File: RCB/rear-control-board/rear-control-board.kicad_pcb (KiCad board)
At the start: 2 copper layers, 99.1 x 99.1 mm, 55 parts, among them J1 Conn_01x23, J2 Conn_01x14, J3 Conn_01x08, J4 Conn_01x02, J5 Conn_01x02, J6 Conn_01x05, K1 T9VV1K15-12S, K2 G5V-2, K3 G5V-2, Q1 BSS84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

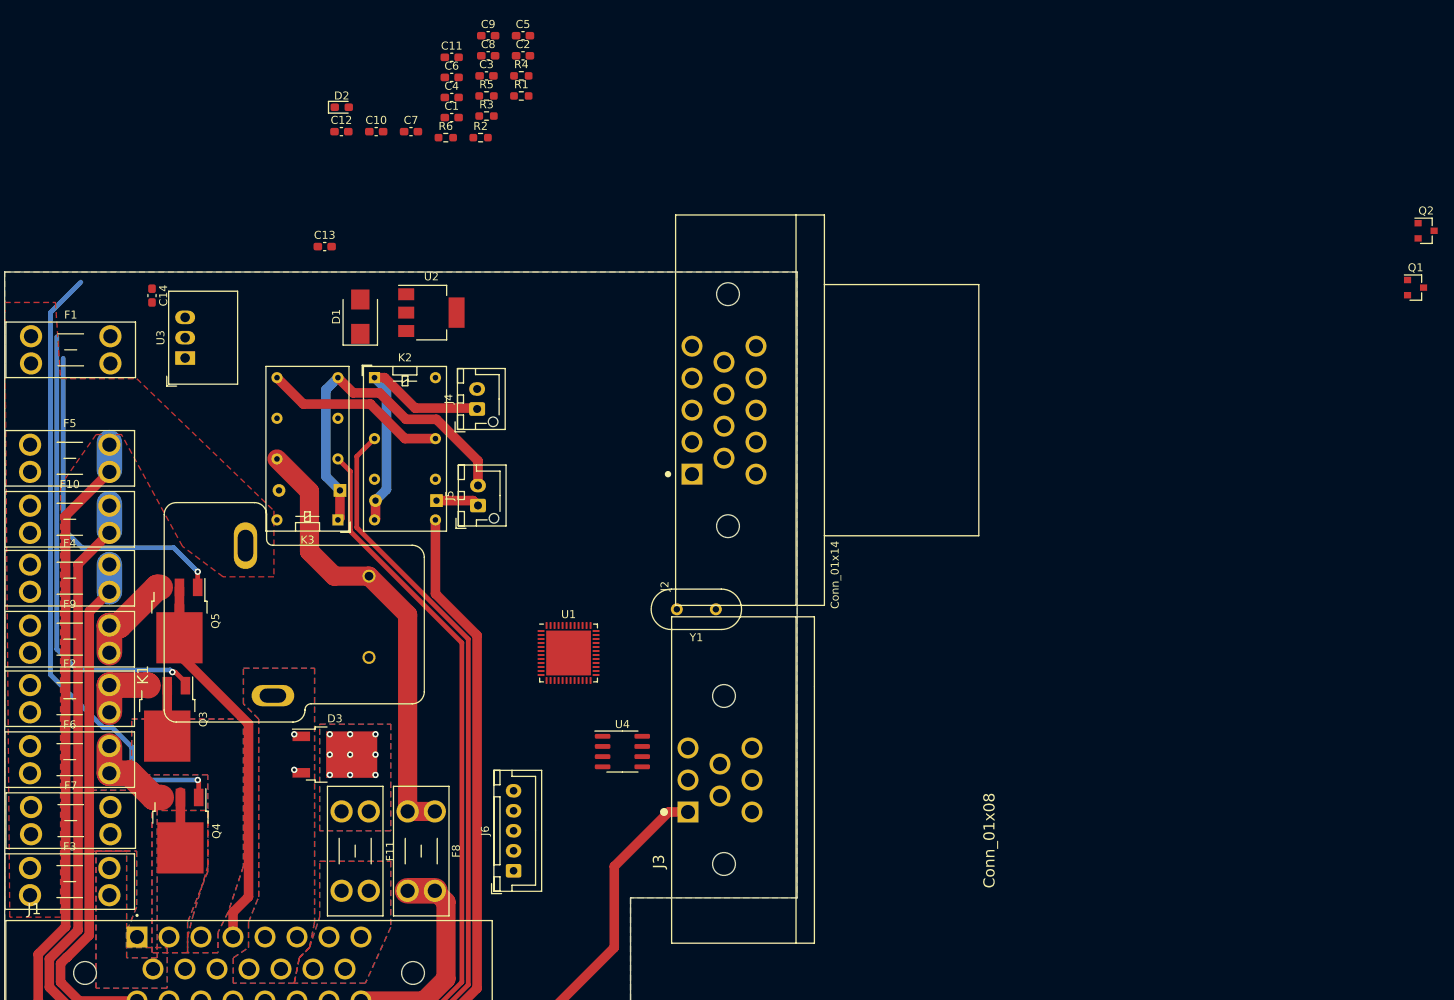
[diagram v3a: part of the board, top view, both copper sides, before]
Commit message: finishing layout placement
Still need to route wires
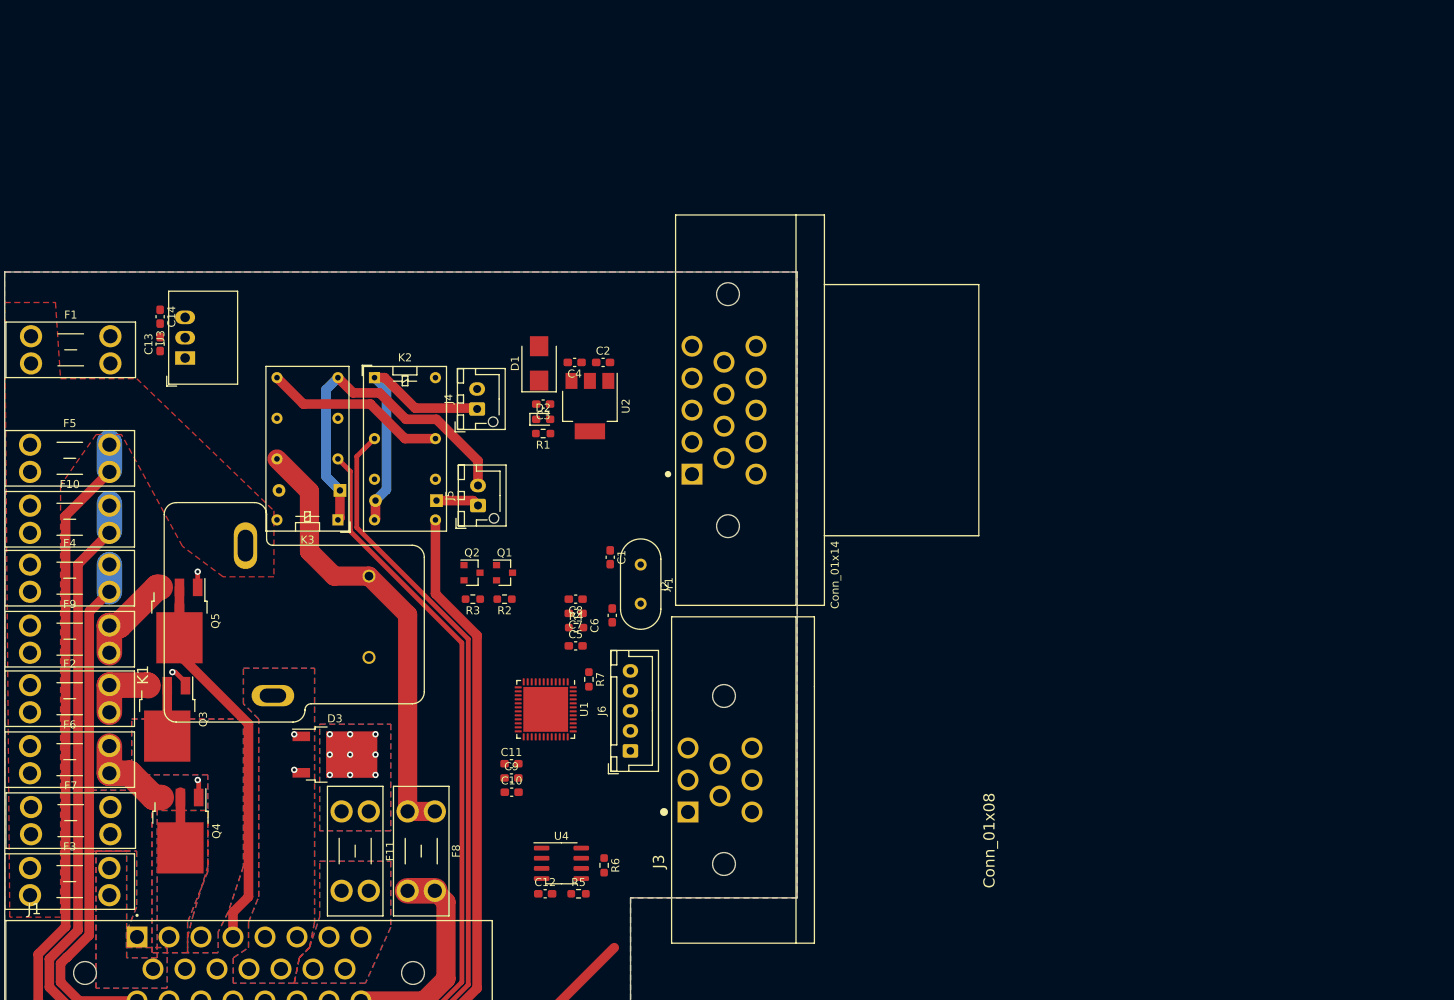
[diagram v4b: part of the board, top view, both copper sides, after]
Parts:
- added R7: 10k, Resistor_SMD:R_0603_1608Metric_Pad0.98x0.95mm_HandSolder, F.Cu at (134.0, 91.6)
- moved Q2 126.7 mm to (119.4, 78.2)
- moved Q1 119.3 mm to (123.4, 78.2)
- moved R5 100.4 mm to (132.7, 118.4)
- moved C12 98.6 mm to (128.5, 118.4)
- moved R6 93.1 mm to (135.9, 114.8), turned to -90 degrees
- moved C9 92.8 mm to (124.3, 103.9)
- moved C11 88.6 mm to (124.3, 102.1)
- moved C10 84.3 mm to (124.3, 105.7)
- moved C5 76.6 mm to (132.3, 87.4)
- moved C6 70.2 mm to (136.9, 83.6), turned to 90 degrees
- moved R4 69.3 mm to (132.4, 85.1)
- moved C8 68.8 mm to (132.3, 81.5), turned to 180 degrees
- moved C7 63.6 mm to (132.3, 83.3), turned to 180 degrees
- moved R3 60.4 mm to (119.5, 81.5), turned to 180 degrees
- moved C1 58.4 mm to (136.7, 76.3), turned to -90 degrees
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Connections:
- J2 pad 1: GND -> /WHEEL_L
- J2 pad 10: /WHEEL_L -> GND
- J2 pad 11: VDD -> GND
- J2 pad 12: VDD -> GND
- J2 pad 13: VDD -> GND
- J2 pad 2: GND -> /WHEEL_R
- J2 pad 3: GND -> +3V3
- J2 pad 4: GND -> VDD
- J2 pad 5: unconnected-(J2-Pad5) -> VDD
- J2 pad 6: /TEMP_WATER -> /TEMP_WATER-
- J2 pad 7: /SUSPENSION_R -> /SUSPENSION_L
- J2 pad 8: /SUSPENSION_L -> /SUSPENSION_R
- J2 pad 9: /WHEEL_R -> VDD
- R2 pad 2: /Controller/FAULT_IMD -> /Controller/FAULT_BMS
- R3 pad 1: /Controller/FAULT_BMS -> /Controller/FAULT_IMD
- U1 pad 14: /Controller/FAN_CTRL -> /Controller/BRAKE_CTRL
- U1 pad 15: /Controller/PUMP_CTRL -> /Controller/FAN_CTRL
- U1 pad 16: /Controller/BRAKE_CTRL -> /Controller/PUMP_CTRL
- U1 pad 17: /Controller/NTC1 -> unconnected-(U1-Pad17)
- U1 pad 18: unconnected-(U1-Pad18) -> /Controller/FAULT_BMS
- U1 pad 19: unconnected-(U1-Pad19) -> /Controller/FAULT_IMD
- U1 pad 2: unconnected-(U1-Pad2) -> /TEMP_WATER-
- U1 pad 32: unconnected-(U1-Pad32) -> /Controller/CAN_X_P
- U1 pad 33: unconnected-(U1-Pad33) -> /Controller/CAN_X_N
- U1 pad 43: /Controller/FAULT_IMD -> unconnected-(U1-Pad43)
- U1 pad 45: /Controller/FAULT_BMS -> unconnected-(U1-Pad45)
- U4 pad 1: /Controller/CAN_TX_P -> /Controller/CAN_X_P
- U4 pad 4: /Controller/CAN_RX_N -> /Controller/CAN_X_N
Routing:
- net /Controller/PUMP_CTRL: track 78.0 -> 2.23 mm
- net /Controller/FAN_CTRL: track 57.3 -> 2.64 mm
- net /Controller/BRAKE_CTRL: track 42.3 -> 1.96 mm
- net /HVB_12V: track 175.7 -> 153.6 mm

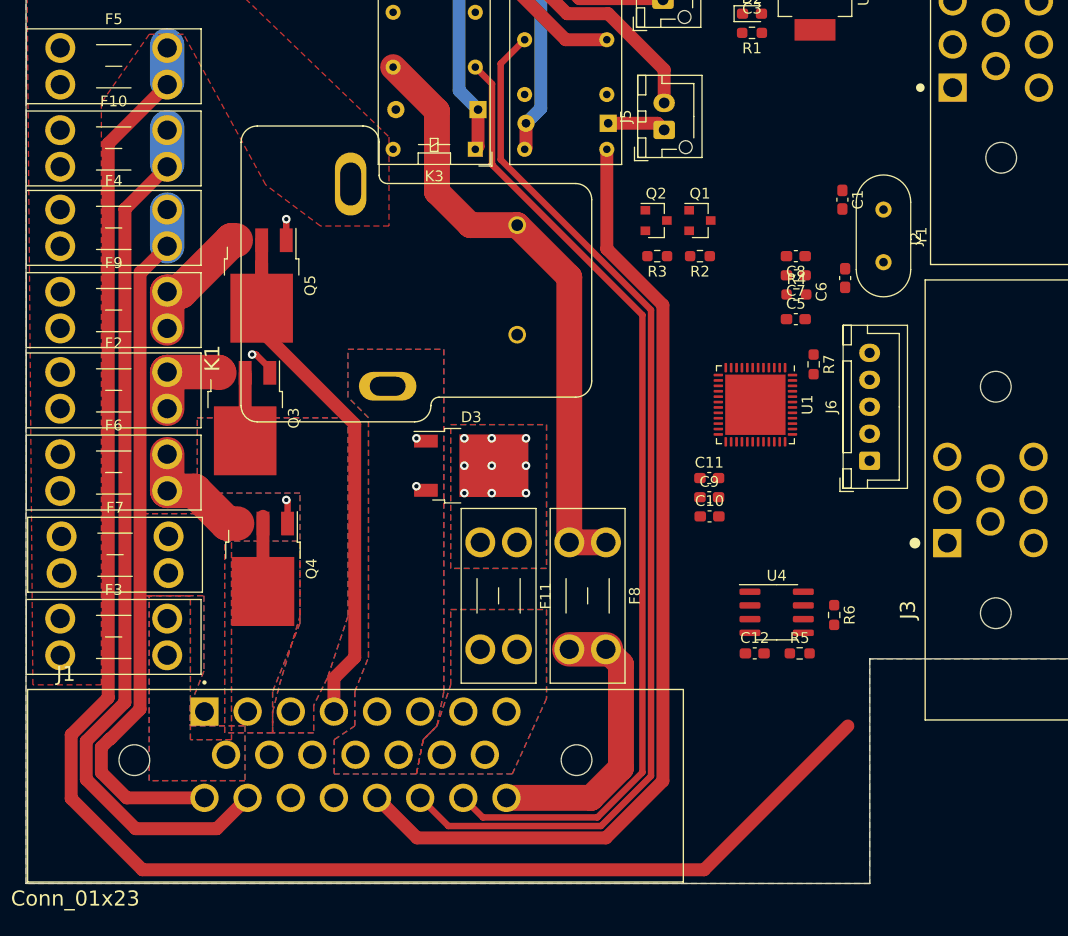
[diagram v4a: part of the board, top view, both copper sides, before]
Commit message: adjusting pinout, updating layout
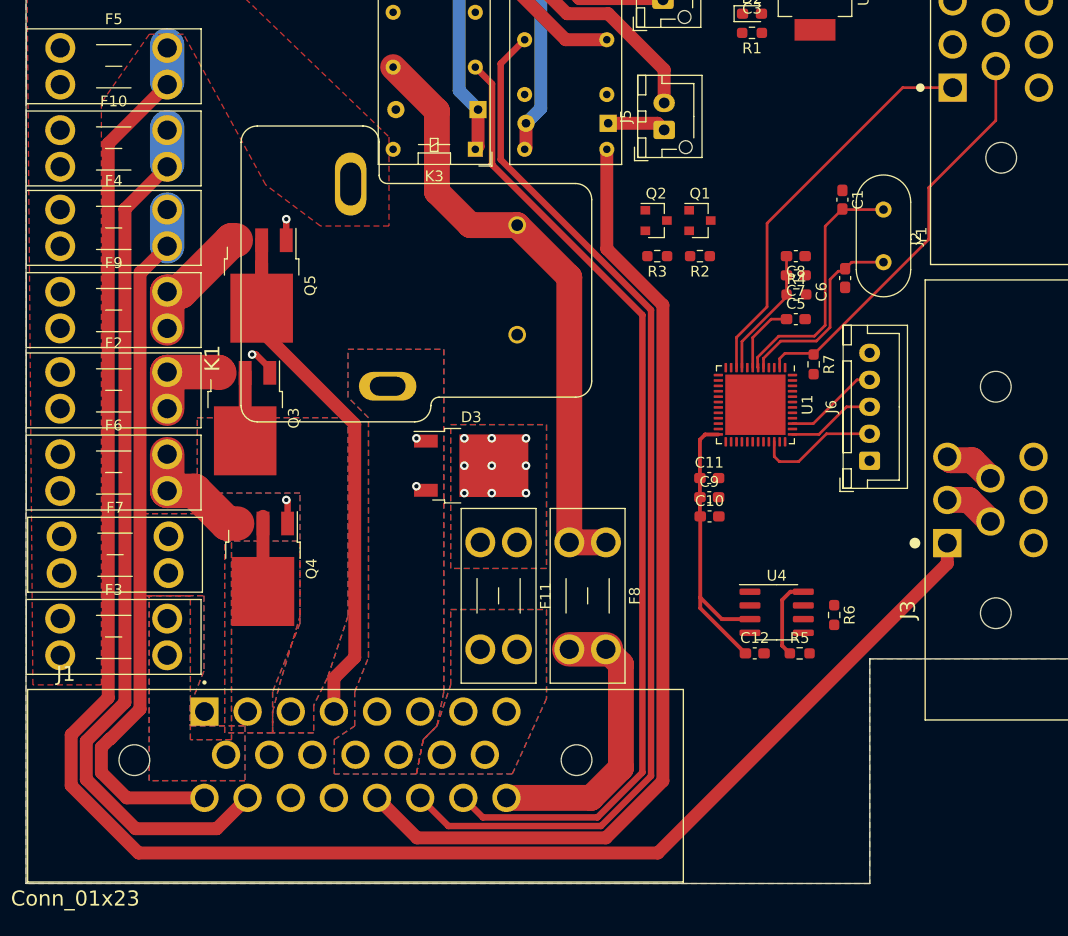
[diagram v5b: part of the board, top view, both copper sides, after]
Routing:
- net /TEMP_WATER-: track 0.00 -> 38.0 mm
- net /WHEEL_L: track 0.00 -> 37.0 mm
- net +3V3: track 0.00 -> 28.9 mm
- net Net-(C1-Pad2): track 0.00 -> 23.8 mm
- net Net-(C6-Pad2): track 0.00 -> 18.3 mm
- net /HVB_12V: track 153.6 -> 168.9 mm
- net Net-(C7-Pad2): track 0.00 -> 12.1 mm
- net A13_SWDIO: track 0.00 -> 11.5 mm
- net B3_TRACESWO: track 0.00 -> 8.83 mm
- net A14_SWCLK: track 0.00 -> 8.21 mm
- net Net-(R5-Pad1): track 0.00 -> 7.53 mm
- net Net-(C5-Pad1): track 0.00 -> 6.63 mm
- net /CAN_P: track 0.00 -> 4.83 mm
- net /CAN_N: track 0.00 -> 4.83 mm

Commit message: trace layout complete (need review)
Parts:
- moved Q1 4.56 mm to (119.0, 77.2), turned to 90 degrees
- moved Q2 4.33 mm to (123.7, 78.5)
- moved Y1 3.21 mm to (140.5, 74.0)
- moved R3 1.24 mm to (119.0, 80.4)
- moved C2 1.12 mm to (135.8, 53.1)
- moved C4 1.12 mm to (132.2, 53.1)
- moved U2 1.12 mm to (134.1, 58.5)
- moved C12 0.76 mm to (129.3, 118.4)
- moved C5 0.72 mm to (131.8, 87.9)
- moved R2 0.62 mm to (123.8, 82.0), turned to 0 degrees
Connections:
- R2 pad 2: /Controller/FAULT_BMS -> /Controller/FAULT_IMD
- R3 pad 1: /Controller/FAULT_IMD -> /Controller/FAULT_BMS
- U1 pad 15: /Controller/FAN_CTRL -> /Controller/PUMP_CTRL
- U1 pad 16: /Controller/PUMP_CTRL -> /Controller/FAN_CTRL
- U1 pad 18: /Controller/FAULT_BMS -> /Controller/FAULT_IMD
- U1 pad 19: /Controller/FAULT_IMD -> /Controller/FAULT_BMS
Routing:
- net +3V3: track 28.9 -> 225.5 mm, vias 0 -> 1
- net VDD: track 5.44 -> 119.5 mm
- net /Controller/PUMP_CTRL: track 2.23 -> 74.2 mm, vias 1 -> 2
- net /SUSPENSION_R: track 0.00 -> 48.7 mm
- net /Controller/FAN_CTRL: track 2.64 -> 47.6 mm, vias 1 -> 2
- net /SUSPENSION_L: track 0.00 -> 44.9 mm
- net /Controller/BRAKE_CTRL: track 1.96 -> 45.4 mm, vias 1 -> 2
- net /WHEEL_R: track 0.00 -> 39.3 mm
- net /Controller/FAULT_BMS: track 0.00 -> 23.6 mm
- net /CAN_N: track 4.83 -> 26.1 mm
- net /Controller/FAULT_IMD: track 0.00 -> 21.2 mm
- net /CAN_P: track 4.83 -> 25.8 mm
- net /Controller/CAN_X_N: track 0.00 -> 19.3 mm
- net /Controller/CAN_X_P: track 0.00 -> 19.1 mm
- net /FAULT_LATCHER/bms_switch: track 33.5 -> 50.9 mm
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- added copper zone on B.Cu, net +12V

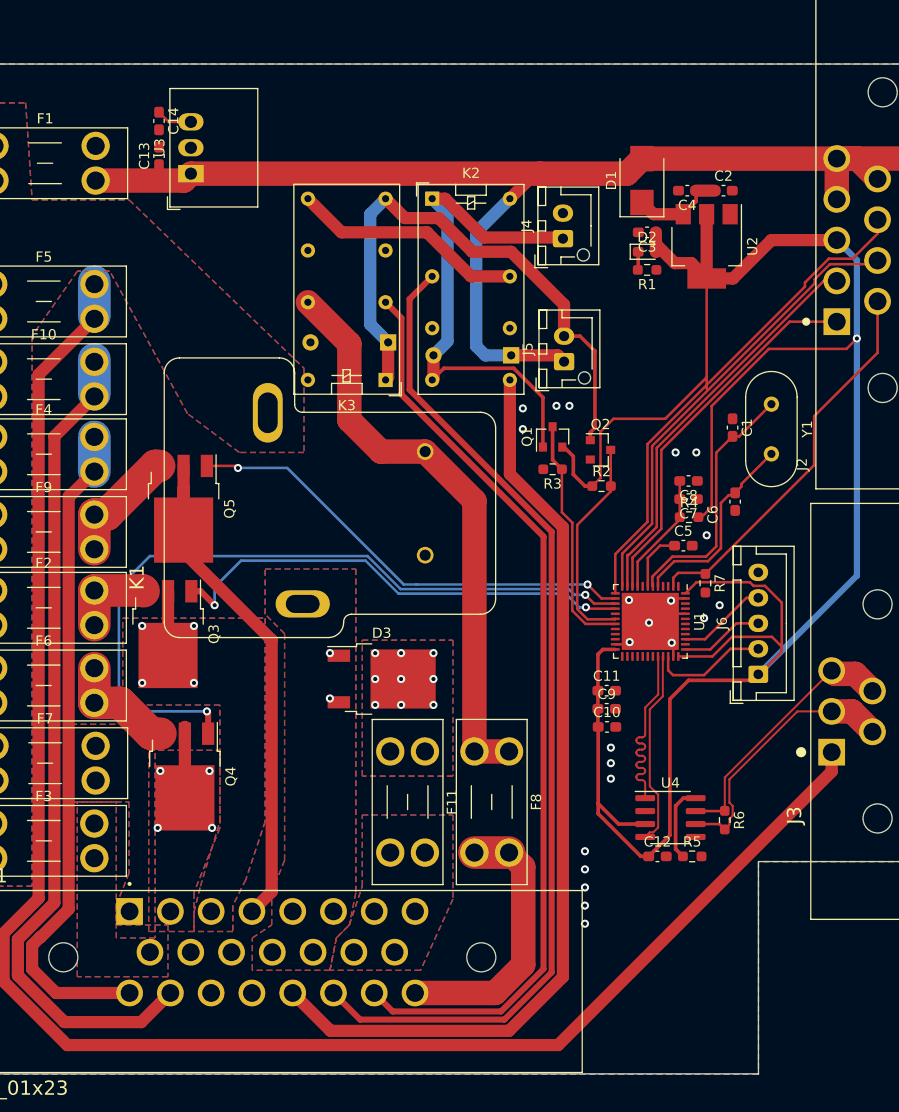
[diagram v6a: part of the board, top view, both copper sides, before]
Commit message: adding mounting holes
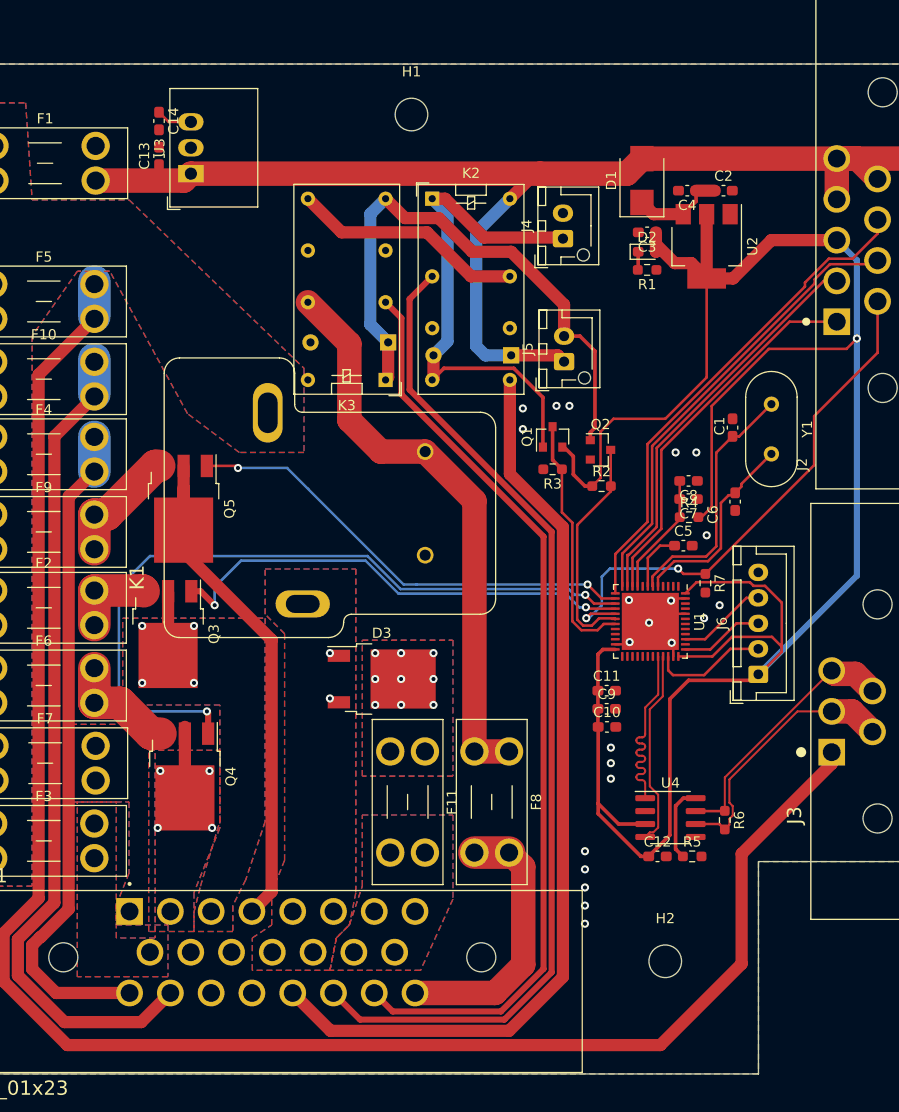
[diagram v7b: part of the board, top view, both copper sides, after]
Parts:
- added H1: MountingHole, MountingHole:MountingHole_3.2mm_M3, F.Cu at (105.2, 45.6)
- added H2: MountingHole, MountingHole:MountingHole_3.2mm_M3, F.Cu at (130.0, 128.7)
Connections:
- U1 pad 17: unconnected-(U1-Pad17) -> /TEMP_WATER-
- U1 pad 2: /TEMP_WATER- -> unconnected-(U1-Pad2)
- U1 pad 38: A15 -> unconnected-(U1-Pad38)
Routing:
- net /TEMP_WATER-: track 38.0 -> 52.5 mm, vias 0 -> 2
- net /HVB_12V: track 168.9 -> 174.8 mm
- net /Controller/FAULT_IMD: track 21.2 -> 22.4 mm
- net +3V3: track 225.5 -> 224.3 mm
- net /Controller/FAULT_BMS: track 23.6 -> 24.7 mm
